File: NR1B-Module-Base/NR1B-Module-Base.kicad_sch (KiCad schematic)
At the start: 1 part, among them X1 NUCLEO144-ZIO

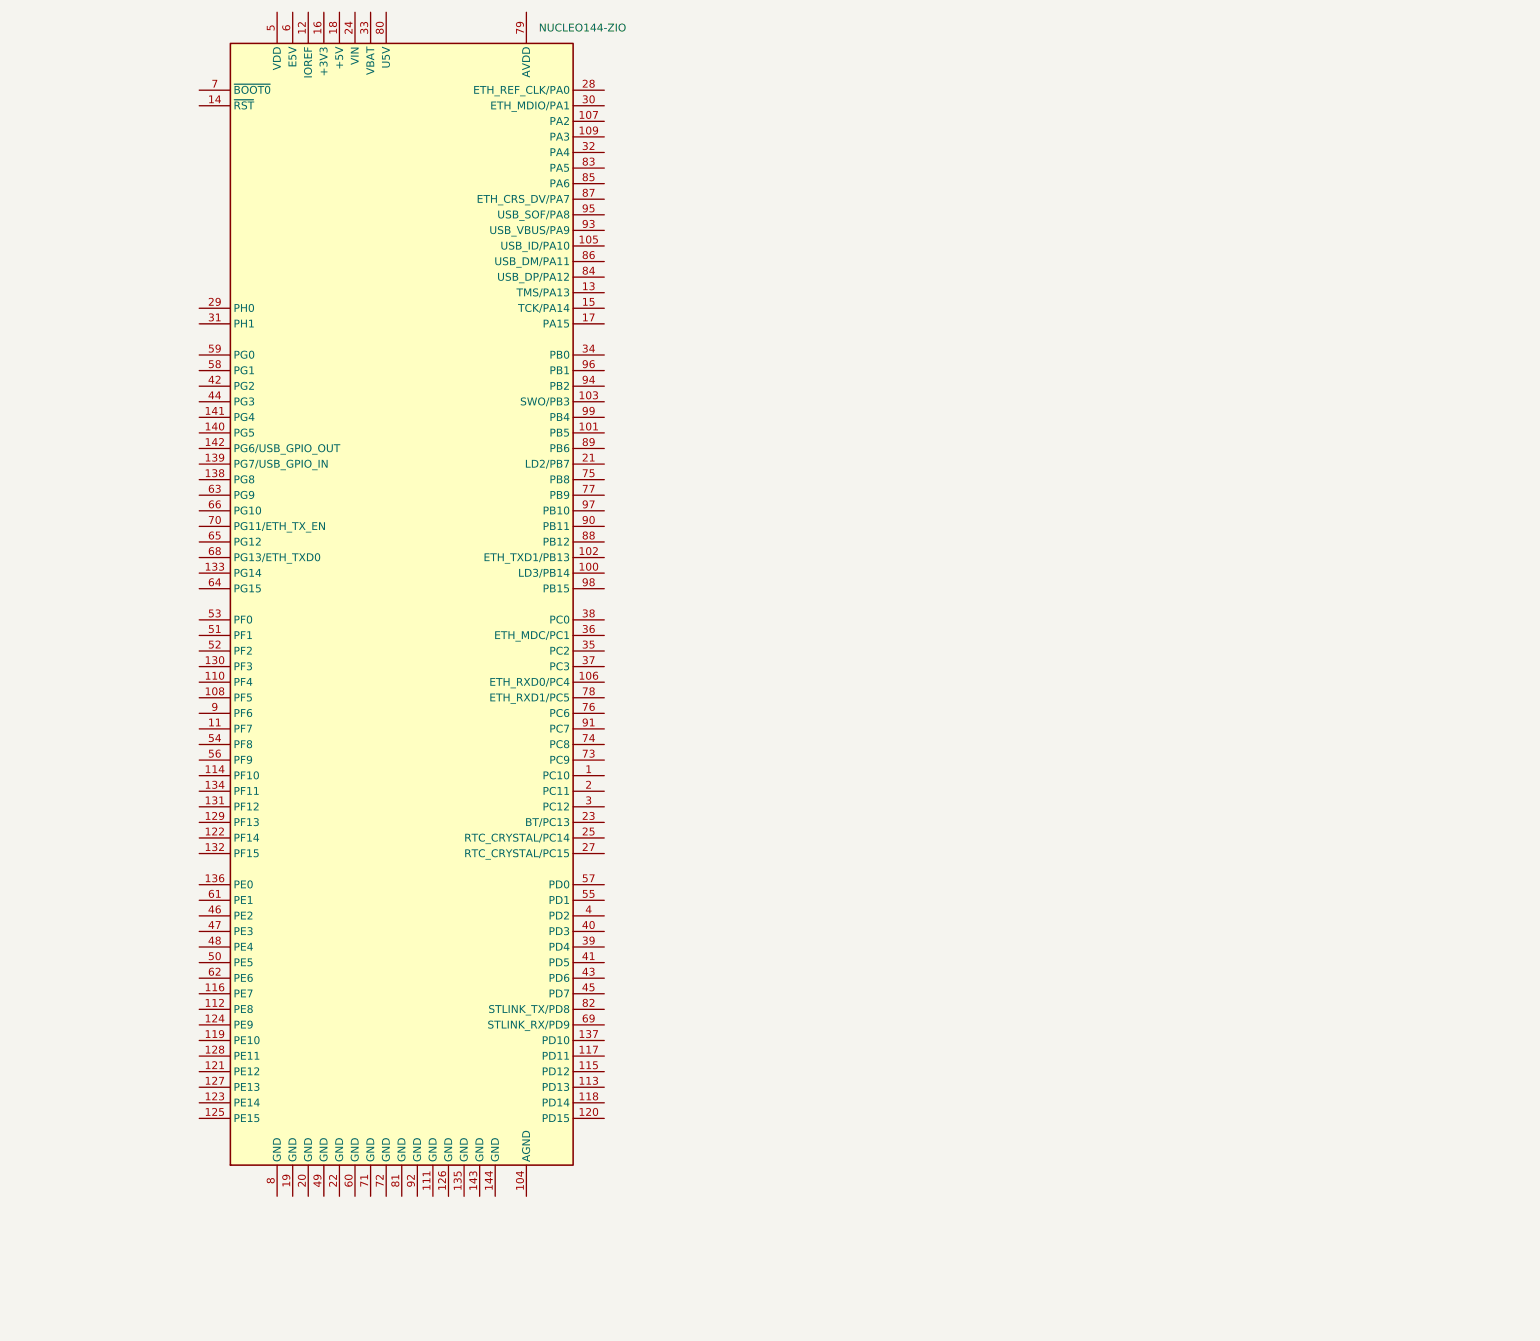
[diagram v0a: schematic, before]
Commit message: Added two 2x4 pin header feedthrough connectors for non-MCU signals
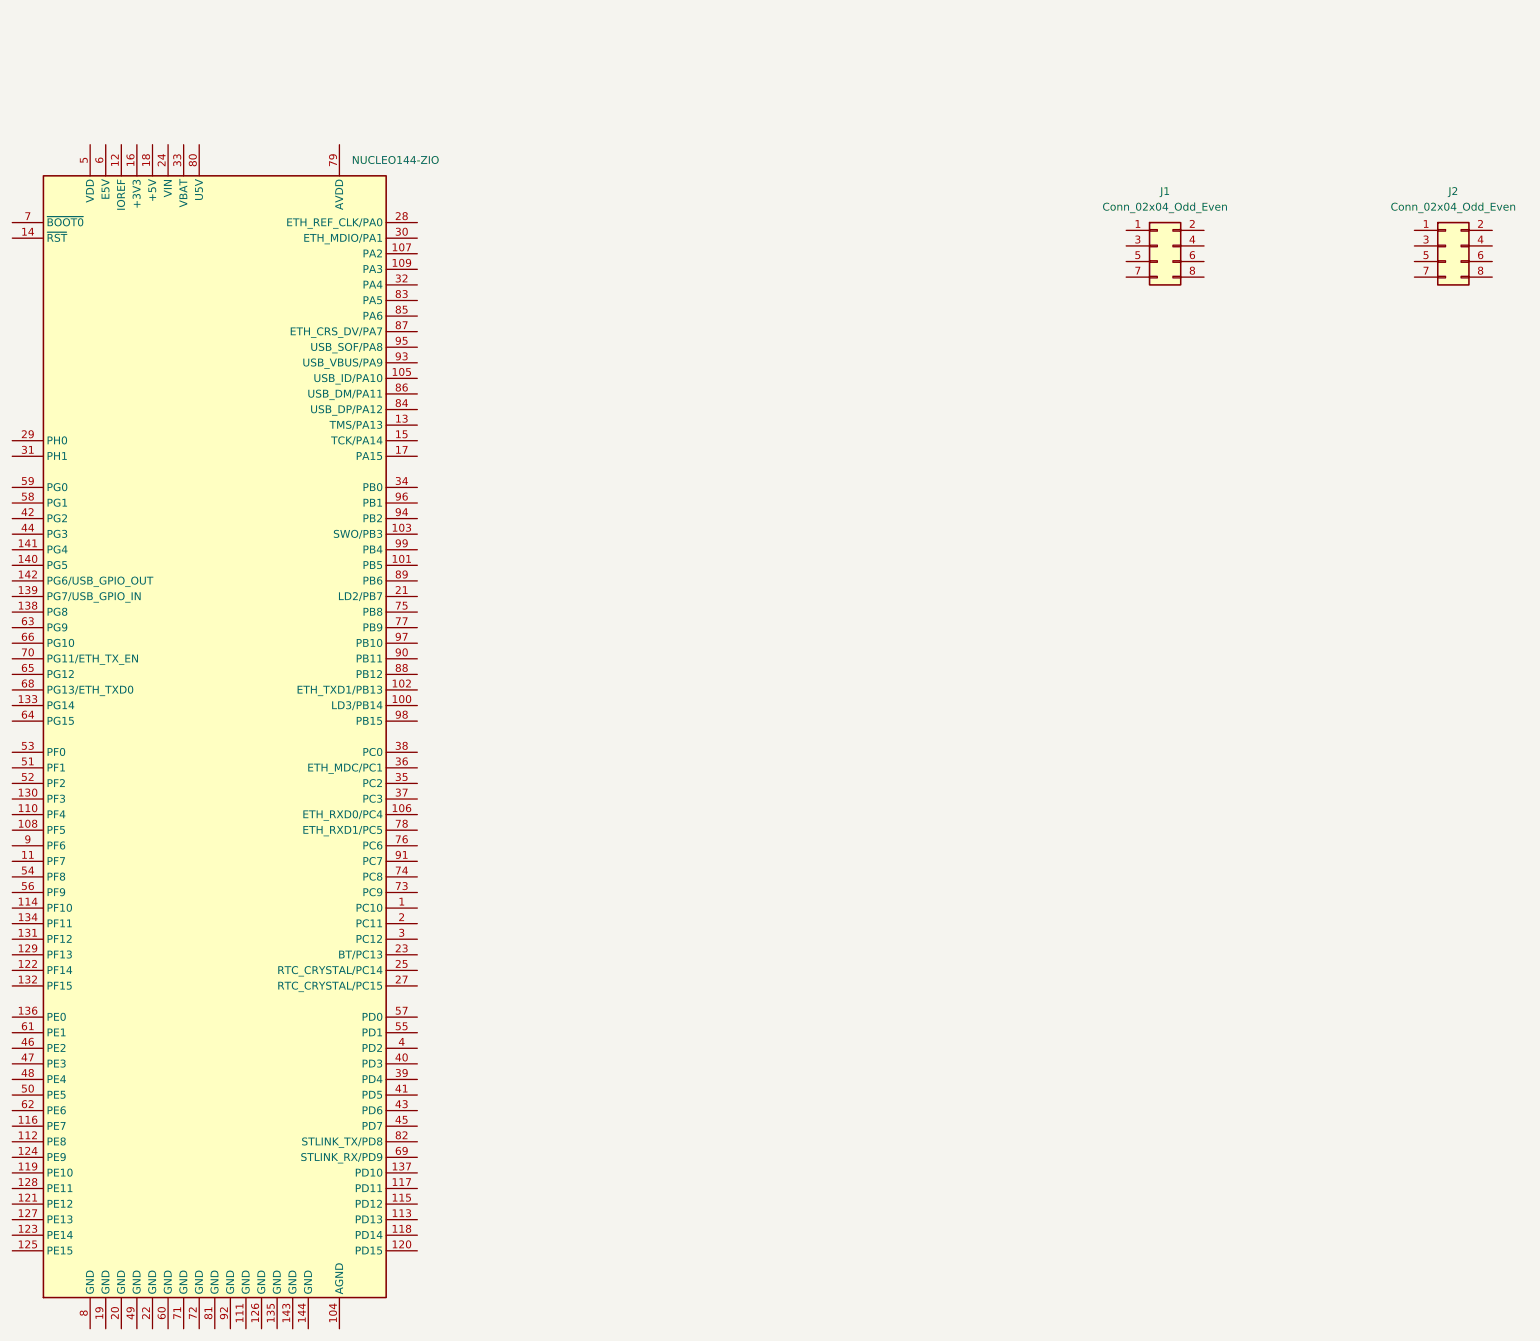
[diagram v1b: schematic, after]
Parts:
- added J1, J2: Conn_02x04_Odd_Even, Connector_PinHeader_2.54mm:PinHeader_2x04_P2.54mm_Vertical, symbol Connector_Generic:Conn_02x04_Odd_Even
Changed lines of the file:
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@@
     (comment 1 "Drawn By: Aidan Medcalf")
   )
-  (symbol (lib_id "NISoC-Socket:NUCLEO144-ZIO") (at 148.59 121.92 0) (unit 1)
+  (symbol (lib_id "Connector_Generic:Conn_02x04_Odd_Even") (at 318.77 63.5 0) (unit 1)
     (in_bom yes) (on_board yes) (fields_autoplaced)
-    (property "Reference" "X1" (id 0) (at 125.73 27.305 0)
+    (property "Reference" "J2" (id 0) (at 320.04 54.61 0))
+    (property "Value" "Conn_02x04_Odd_Even" (id 1) (at 320.04 57.15 0))
+    (property "Footprint" "Connector_PinHeader_2.54mm:PinHeader_2x04_P2.54mm_Vertical" (id 2) (at 318.77 63.5 0)
+      (effects (font (size 1.27 1.27)) hide)
+    )
+    (property "Datasheet" "~" (id 3) (at 318.77 63.5 0)
+      (effects (font (size 1.27 1.27)) hide)
+    )
+    (pin "1")
+    (pin "2")
+    (pin "3")
+    (pin "4")
+    (pin "5")
+    (pin "6")
+    (pin "7")
+    (pin "8")
+  )
+  (symbol (lib_id "NISoC-Socket:NUCLEO144-ZIO") (at 118.11 143.51 0) (unit 1)
+    (in_bom yes) (on_board yes) (fields_autoplaced)
+    (property "Reference" "X1" (id 0) (at 95.25 48.895 0)
       (effects (font (size 1.27 1.27)) (justify right) hide)
     )
-    (property "Value" "NUCLEO144-ZIO" (id 1) (at 170.9294 27.94 0)
+    (property "Value" "NUCLEO144-ZIO" (id 1) (at 140.4494 49.53 0)
       (effects (font (size 1.27 1.27)) (justify left))
     )
-    (property "Footprint" "NISoC-Socket:ST_Morpho_Connector_144_STLink_MountingHoles" (id 2) (at 170.18 214.63 0)
+    (property "Footprint" "NISoC-Socket:ST_Morpho_Connector_144_STLink_MountingHoles" (id 2) (at 139.7 236.22 0)
       (effects (font (size 1.27 1.27)) (justify left) hide)
     )
-    (property "Datasheet" "" (id 3) (at 125.73 114.3 0)
+    (property "Datasheet" "" (id 3) (at 95.25 135.89 0)
       (effects (font (size 1.27 1.27)) hide)
     )
@@
     (pin "99")
   )
+  (symbol (lib_id "Connector_Generic:Conn_02x04_Odd_Even") (at 271.78 63.5 0) (unit 1)
+    (in_bom yes) (on_board yes) (fields_autoplaced)
+    (property "Reference" "J1" (id 0) (at 273.05 54.61 0))
+    (property "Value" "Conn_02x04_Odd_Even" (id 1) (at 273.05 57.15 0))
+    (property "Footprint" "Connector_PinHeader_2.54mm:PinHeader_2x04_P2.54mm_Vertical" (id 2) (at 271.78 63.5 0)
+      (effects (font (size 1.27 1.27)) hide)
+    )
+    (property "Datasheet" "~" (id 3) (at 271.78 63.5 0)
+      (effects (font (size 1.27 1.27)) hide)
+    )
+    (pin "1")
+    (pin "2")
+    (pin "3")
+    (pin "4")
+    (pin "5")
+    (pin "6")
+    (pin "7")
+    (pin "8")
+  )
   (sheet_instances
     (path "/" (page "1"))
   )
   (symbol_instances
+    (path "/c17ae2ea-c320-4586-86b4-0b8496adc1a9"
+      (reference "J1") (unit 1) (value "Conn_02x04_Odd_Even") (footprint "Connector_PinHeader_2.54mm:PinHeader_2x04_P2.54mm_Vertical")
+    )
+    (path "/48e1a80a-7278-460b-b182-18809159e44a"
+      (reference "J2") (unit 1) (value "Conn_02x04_Odd_Even") (footprint "Connector_PinHeader_2.54mm:PinHeader_2x04_P2.54mm_Vertical")
+    )
     (path "/7d155246-7238-41dc-89ca-cec5d7d04db9"
       (reference "X1") (unit 1) (value "NUCLEO144-ZIO") (footprint "NISoC-Socket:ST_Morpho_Connector_144_STLink_MountingHoles")
